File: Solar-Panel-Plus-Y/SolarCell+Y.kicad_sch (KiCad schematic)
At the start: 66 parts, among them J1 symbols_XF2M-1015-1A, J2 U.FL-R-SMT-1, Q1 IRLML2803, U1 TTB12G51-Balun, U2 NDS8434, U3 TSL2561, U4 Value

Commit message: More Cleanup
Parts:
- D1, D2: symbol SolarCell+Y-rescue:SBDiode-SolarCellParts -> SolarCellParts:SBDiode
- D3: footprint MICROSMP -> misc-circuits:MICROSMP; symbol SolarCell+Y-rescue:MSS1P4-M3_89A-symbols -> Device:D_Schottky
- D4: symbol SolarCellX_v3-rescue:MSS1P4-M3_89A-symbols -> Device:D_Schottky
- D5: footprint misc-circuits:SOD523 -> Diode_SMD:D_SOD-523; symbol SolarCellX_v3-rescue:DIODE-SOD523-misc-circuits-cache-misc-circuits-rescue -> Device:D
- J1: footprint XF2M-1015-1A -> misc-circuits:XF2M-1015-1A; symbol SolarCell+Y-rescue:symbols_XF2M-1015-1A-misc-circuits-cache -> misc-circuits-cache:symbols_XF2M-1015-1A
- J2: footprint U.FL-R-SMT-1 -> misc-circuits:U.FL-R-SMT-1; symbol SolarCell+Y-rescue:U.FL-R-SMT-1-symbols -> Hirose U.FL-R-SMT-1:U.FL-R-SMT-1-symbols
- JP1: footprint custom-footprints:Burn-Wire -> SolarCellParts:Burn Wire; symbol Device:Jumper -> misc-circuits-cache:Device_Jumper
- L1, L2: symbol SolarCellX_v3-rescue:COILCRAFT-LPS4018-misc-circuits-cache-misc-circuits-rescue -> misc-circuits-cache:misc-circuits-rescue_COILCRAFT-LPS4018-misc-circuits-cache
- Q1: symbol SolarCell+Y-rescue:IRLML2803TRPBF-mainboard-misc-circuits-rescue-SolarCellZ_v1-rescue -> misc-circuits-cache:misc-circuits-rescue_IRLML2803TRPBF-mainboard
- U1: footprint custom-footprints:2450FM07D0034T -> misc-circuits:TTB12G51-balun; symbol SolarCell+Y-rescue:TTB12G51-Balun-symbols -> Device:Transformer_1P_1S
- U2: footprint custom-footprints:NDS8434 -> misc-circuits:NDS8434; symbol SolarCell+Y-rescue:NDS8434-symbols-misc-circuits-rescue-SolarCellZ_v1-rescue -> misc-circuits-cache:symbols_NDS8434
- U3: footprint custom-footprints:TSL2561 -> misc-circuits:TSL2561; symbol SolarCell+Y-rescue:TSL2561-symbols -> misc-circuits-cache:symbols_TSL2561
- U4: symbol SolarCellX_v3-rescue:BQ25570RGRR-misc-circuits-cache-misc-circuits-rescue -> misc-circuits-cache:misc-circuits-rescue_BQ25570RGRR-misc-circuits-cache
- gave numbers to parts that had none: 1
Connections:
- net GND: now also D5.2 (A); no longer D5.A, U1.5 (GND)
- net VSOLAR: now also D5.1 (K); no longer D5.C
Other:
- note added: "Coil"
- note added: "Flat Flex Connector"
- note added: "Light Sensor"
- note added: "Solar Cells"
- note removed: "Power and Connectors"
- note removed: "Solar"
- title: (none) -> Solar Panel Board +Y
- moved on the sheet: C1, C11, C12, C14, C15, C2, C8, D1, D2, H1, H2, J1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

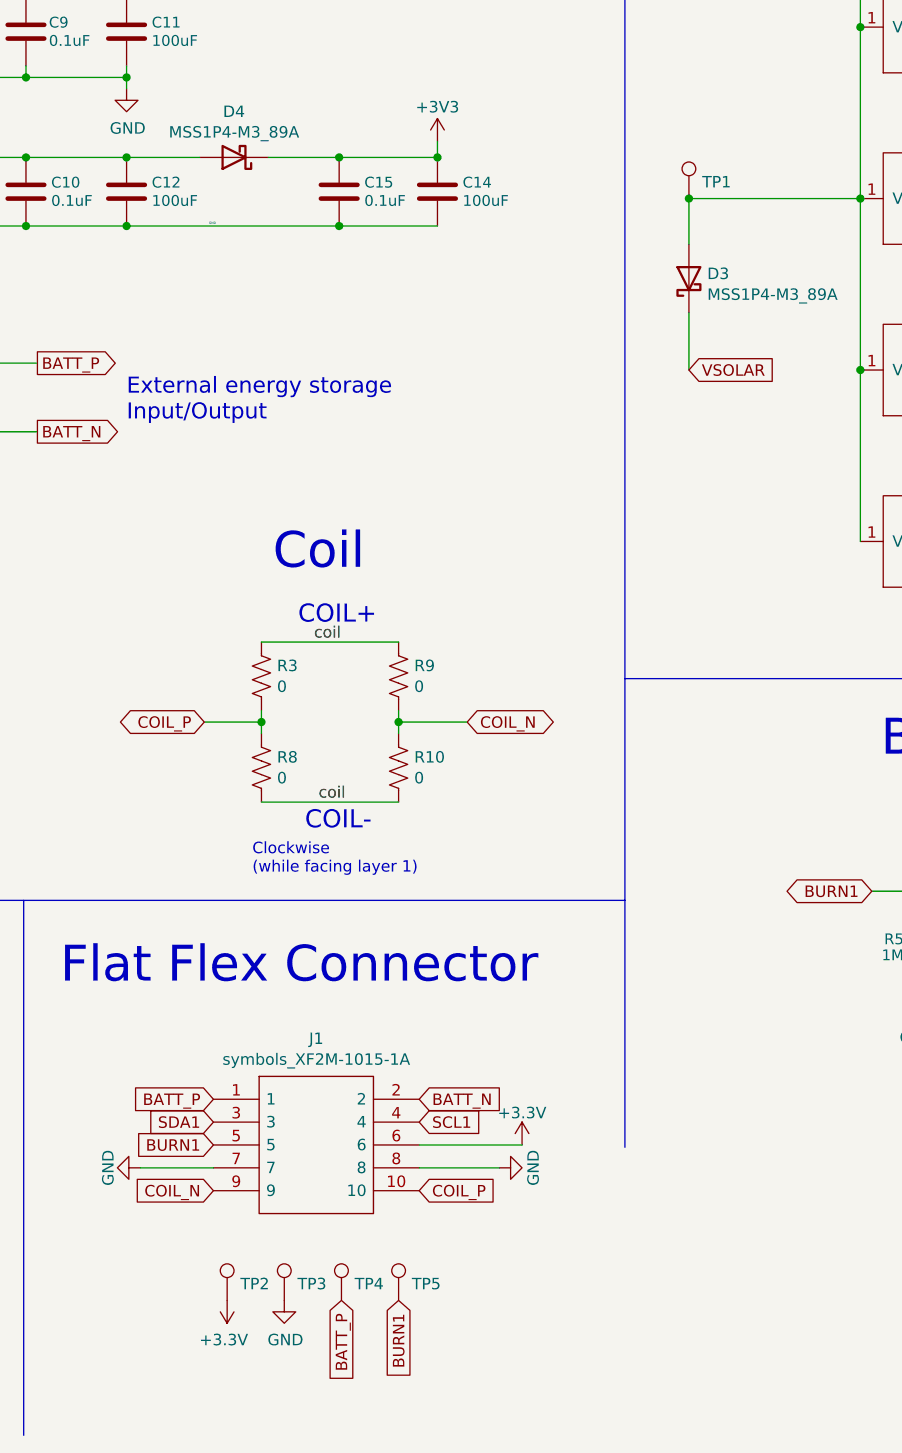
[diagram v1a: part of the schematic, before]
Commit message: Moved board connectors to North board edges
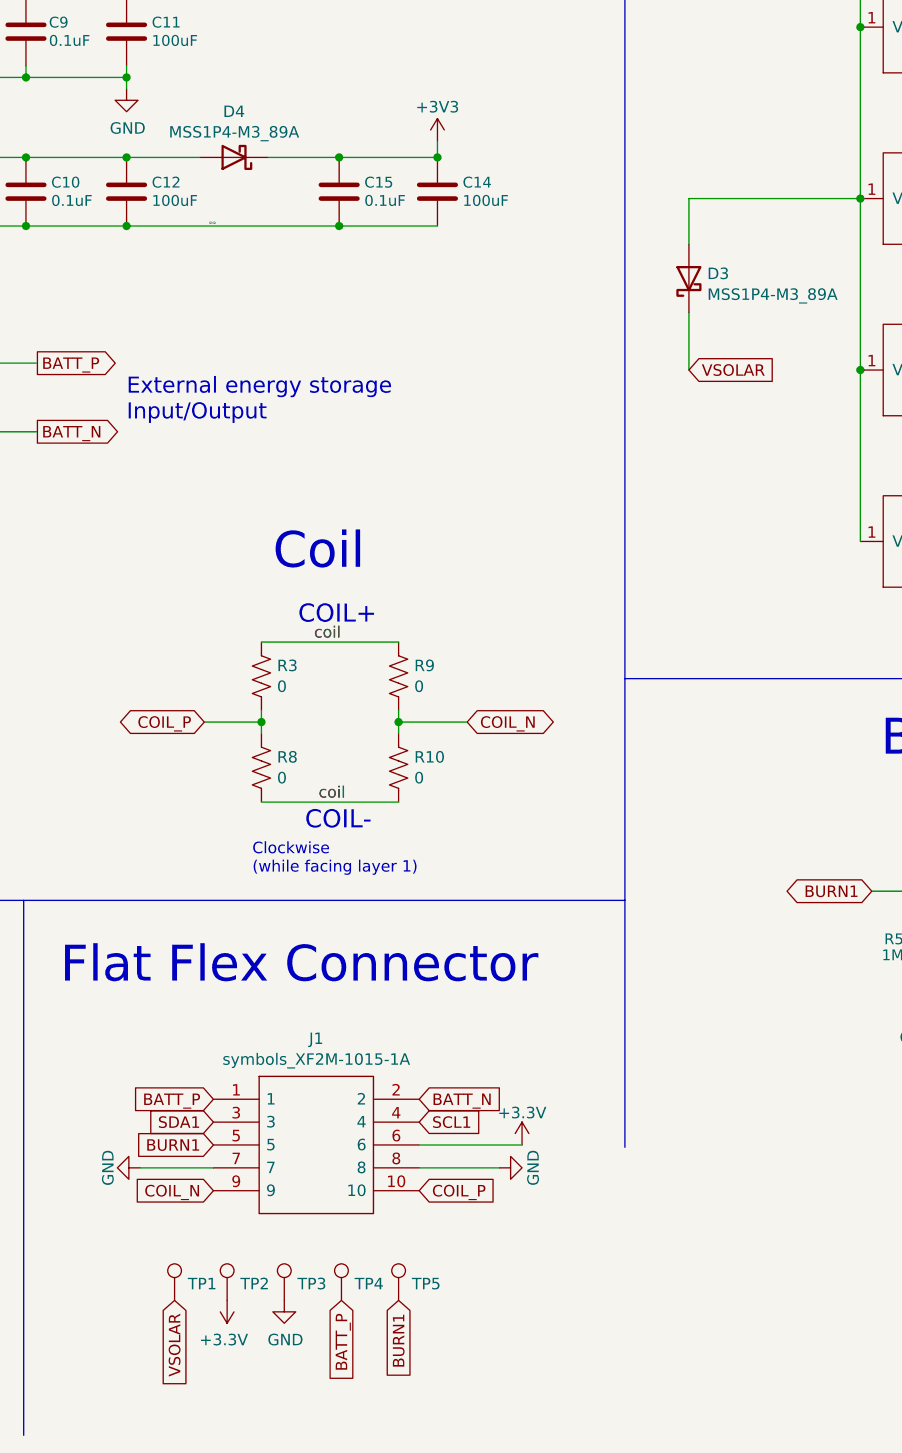
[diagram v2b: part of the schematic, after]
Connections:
- net VSOLAR: now also TP1.1
- net at D1.1 (NEG), D3.2 (A), SC1.1 (V+)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: no longer TP1.1
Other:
- moved on the sheet: TP1
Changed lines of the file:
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@@
   (junction (at 336.296 66.548) (diameter 0) (color 0 0 0 0)
-  )
-  (junction (at 242.824 66.548) (diameter 0) (color 0 0 0 0)
   )
   (junction (at 159.004 69.596) (diameter 0) (color 0 0 0 0)
@@
     (effects (font (size 1.27 1.27)) (justify left))
     (property "Intersheet References" "${INTERSHEET_REFS}" (id 0) (at -20.066 8.636 0)
+      (effects (font (size 1.27 1.27)) hide)
+    )
+  )
+  (global_label "VSOLAR" (shape input) (at 185.674 188.976 270) (fields_autoplaced)
+    (effects (font (size 1.27 1.27)) (justify right))
+    (property "Intersheet References" "${INTERSHEET_REFS}" (id 0) (at 334.264 16.256 0)
       (effects (font (size 1.27 1.27)) hide)
     )
@@
     (pin "1")
   )
-  (symbol (lib_id "Connector:TestPoint") (at 242.824 66.548 0) (unit 1)
-    (in_bom yes) (on_board yes)
-    (property "Reference" "TP1" (id 0) (at 244.2972 64.7192 0)
-      (effects (font (size 1.27 1.27)) (justify left))
-    )
-    (property "Value" "TP" (id 1) (at 244.2972 65.8622 0)
-      (effects (font (size 1.27 1.27)) (justify left) hide)
-    )
-    (property "Footprint" "TestPoint:TestPoint_THTPad_D1.0mm_Drill0.5mm" (id 2) (at 247.904 66.548 0)
-      (effects (font (size 1.27 1.27)) hide)
-    )
-    (property "Datasheet" "~" (id 3) (at 247.904 66.548 0)
-      (effects (font (size 1.27 1.27)) hide)
-    )
+  (symbol (lib_id "Connector:TestPoint") (at 185.674 188.976 0) (unit 1)
+    (in_bom yes) (on_board yes)
+    (property "Reference" "TP1" (id 0) (at 187.1472 187.1472 0)
+      (effects (font (size 1.27 1.27)) (justify left))
+    )
+    (property "Value" "TP" (id 1) (at 187.1472 188.2902 0)
+      (effects (font (size 1.27 1.27)) (justify left) hide)
+    )
+    (property "Footprint" "TestPoint:TestPoint_THTPad_D1.0mm_Drill0.5mm" (id 2) (at 190.754 188.976 0)
+      (effects (font (size 1.27 1.27)) hide)
+    )
+    (property "Datasheet" "~" (id 3) (at 190.754 188.976 0)
+      (effects (font (size 1.27 1.27)) hide)
+    )

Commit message: Made Requested Changes
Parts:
- removed H1, H2: MountingHole_Pad, MountingHole:MountingHole_2.2mm_M2_Pad, symbol Mechanical:MountingHole_Pad
- removed J2: U.FL-R-SMT-1, misc-circuits:U.FL-R-SMT-1, symbol Hirose U.FL-R-SMT-1:U.FL-R-SMT-1-symbols
- removed JP1: Jumper, SolarCellParts:Burn Wire, symbol misc-circuits-cache:Device_Jumper
- removed Q1: IRLML2803, Package_TO_SOT_SMD:SOT-23, symbol misc-circuits-cache:misc-circuits-rescue_IRLML2803TRPBF-mainboard
- removed R5, R7: 1M, Resistor_SMD:R_0402_1005Metric, symbol Device:R_US
- removed R6: 4.7k, Resistor_SMD:R_0402_1005Metric, symbol Device:R_US
- removed TP5: TP, TestPoint:TestPoint_THTPad_D1.0mm_Drill0.5mm, symbol Connector:TestPoint
- removed U1: TTB12G51-Balun, misc-circuits:TTB12G51-balun, symbol Device:Transformer_1P_1S
- removed U2: NDS8434, misc-circuits:NDS8434, symbol misc-circuits-cache:symbols_NDS8434
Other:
- note added: "Solar Panel Board +Y"
- note added: "Test Points"
- note removed: "Burnwire Control"
- note removed: "Radio Assembly"
- company: (none) -> REx Lab Carnegie Mellon University
- title: Solar Panel Board +Y -> PyCubed Mini
- moved on the sheet: C1, J1, R1, R10, R2, R3, R8, R9, TP1, TP2, TP3, TP4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
